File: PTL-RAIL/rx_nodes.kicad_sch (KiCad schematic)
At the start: 0 parts

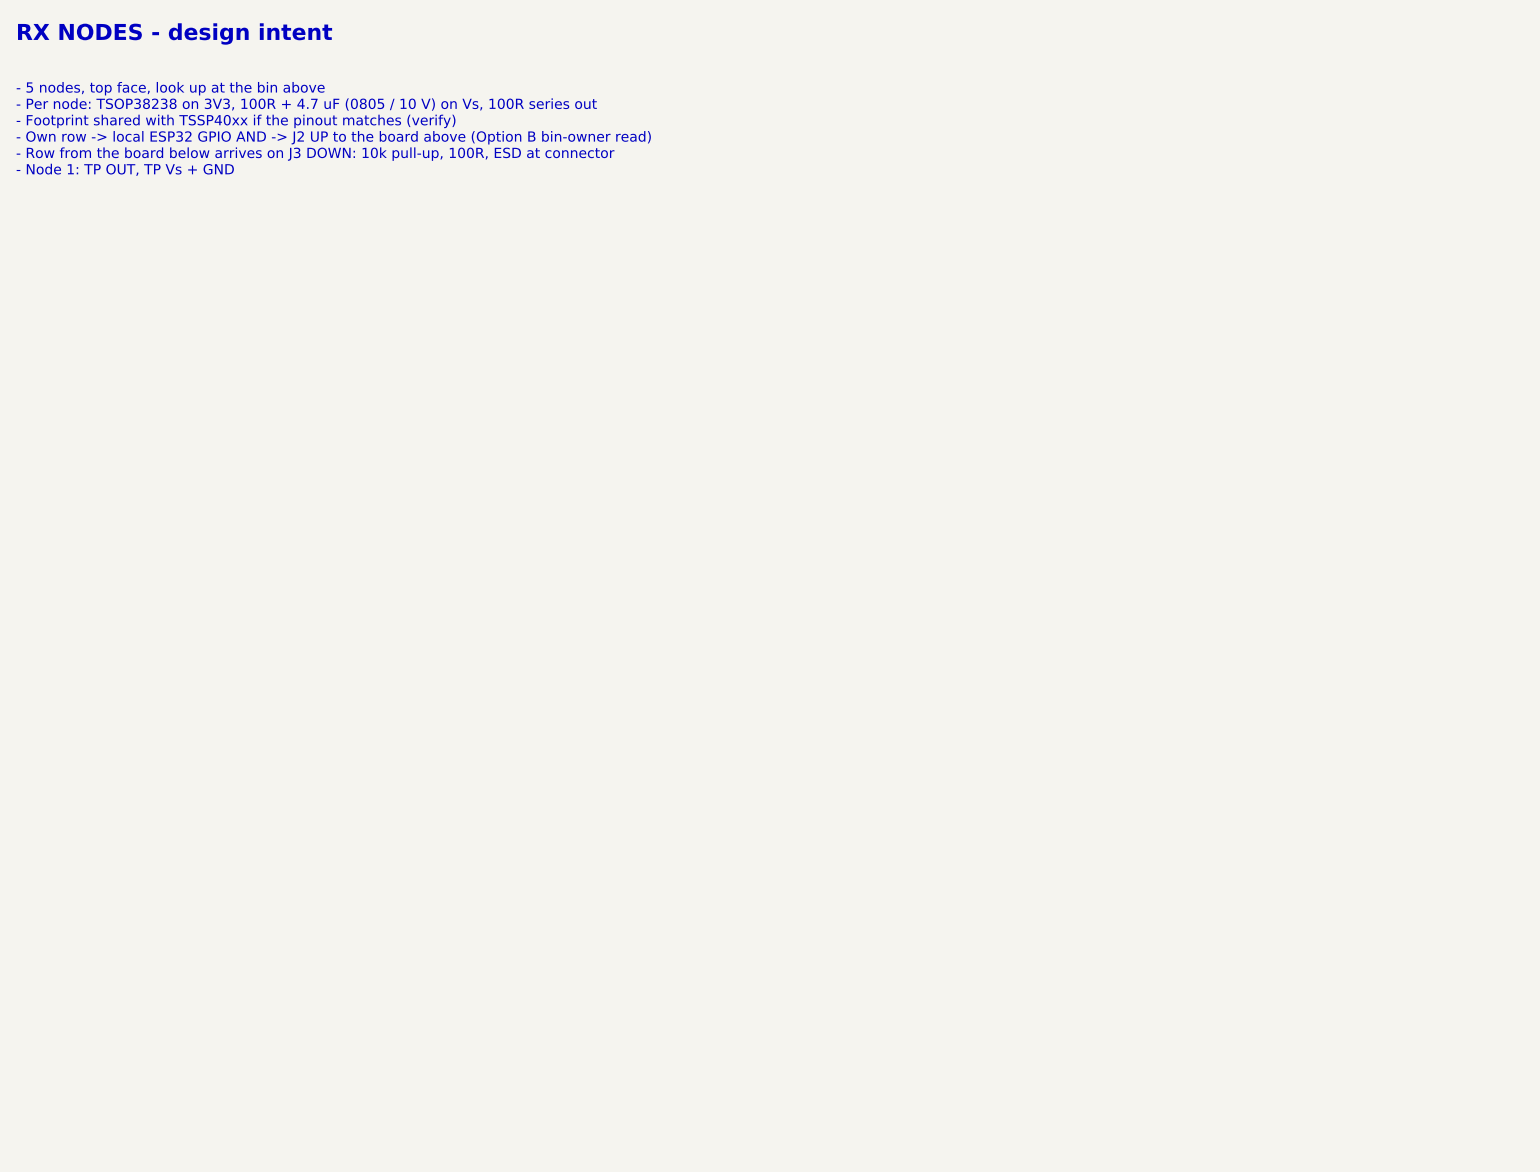
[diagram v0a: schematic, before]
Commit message: PTL-RAIL: LED row on top edge, TSOP row on bottom edge, node parts aligned at 84 mm pitch; J3/J4 10-way and J5/J6 4-way screw terminals
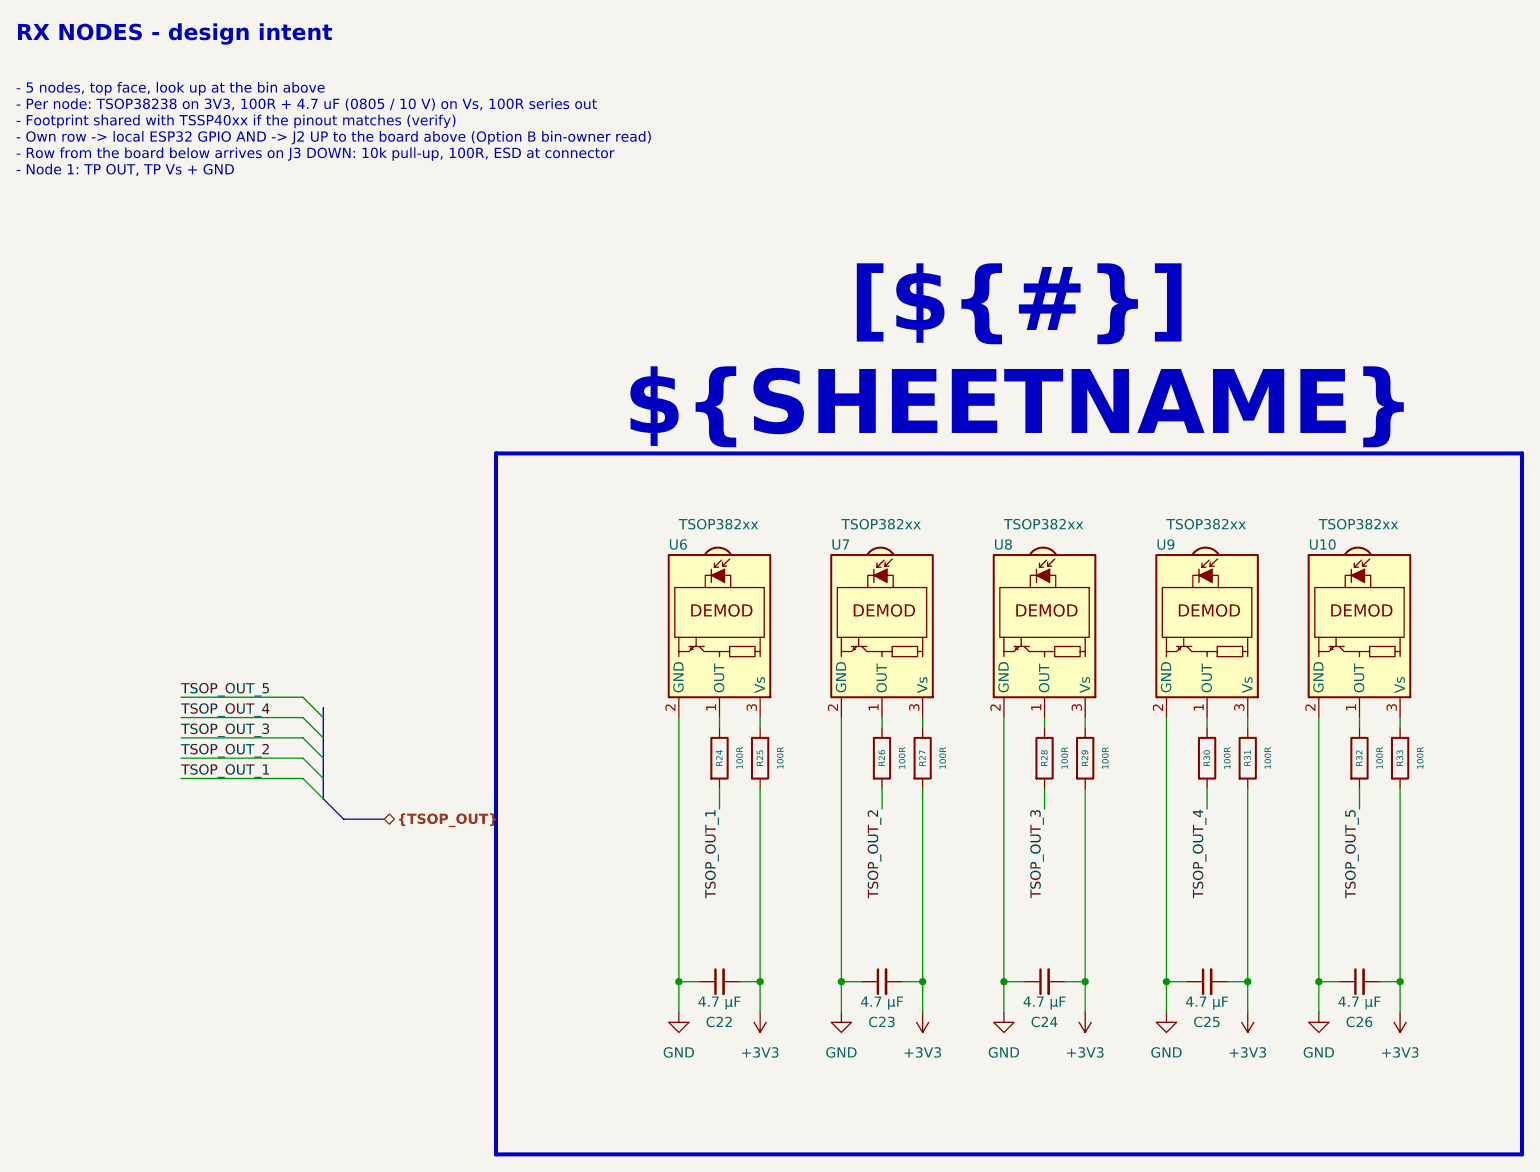
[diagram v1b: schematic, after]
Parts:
- added C22, C23, C24, C25, C26: 4.7 µF, Capacitor_SMD:C_0805_2012Metric, symbol Device:C_Small
- added R24, R25, R26, R27, R28, R29, R30, R31, R32, R33: 100R, Resistor_SMD:R_0805_2012Metric, symbol Device:R
- added U10, U6, U7, U8, U9: TSOP382xx, OptoDevice:Vishay_MINICAST-3Pin, symbol Interface_Optical:TSOP382xx
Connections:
- new net: R26.1, U7.1 (OUT)
- new net: R27.1, U7.3 (Vs)
- new net: R28.1, U8.1 (OUT)
- new net: R29.1, U8.3 (Vs)
- new net: R32.1, U10.1 (OUT)
- new net: R31.1, U9.3 (Vs)
- new net: R33.1, U10.3 (Vs)
- new net: R30.1, U9.1 (OUT)
- new net: R24.1, U6.1 (OUT)
- new net: R25.1, U6.3 (Vs)
- new net +3V3: C22.2, C23.2, C24.2, C25.2, C26.2, R25.2, R27.2, R29.2, R31.2, R33.2
- new net GND: C22.1, C23.1, C24.1, C25.1, C26.1, U10.2 (GND), U6.2 (GND), U7.2 (GND), U8.2 (GND), U9.2 (GND)
- new net TSOP_OUT_1: R24.2
- new net TSOP_OUT_2: R26.2
- new net TSOP_OUT_3: R28.2
- new net TSOP_OUT_4: R30.2
- new net TSOP_OUT_5: R32.2

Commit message: PTL-RAIL: TSOP Vs decoupling caps on the Vs node; place CAN, buttons, status LED and mounting holes
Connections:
- net +3V3: no longer C22.2, C23.2, C24.2, C25.2, C26.2
- net at R27.1, U7.3 (Vs): now also C23.2
- net at R29.1, U8.3 (Vs): now also C24.2
- net at R31.1, U9.3 (Vs): now also C25.2
- net at R33.1, U10.3 (Vs): now also C26.2
- net at R25.1, U6.3 (Vs): now also C22.2
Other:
- moved on the sheet: R25, R27, R29, R31, R33

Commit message: PTL-RAIL rev A: normalize cap values, IO45 no-connect, README and docs
- Capacitor values unified: 0.1uF -> 100nF (C10, C16-C21, C27; now one
  BOM line with C5), '4.7 µF' -> 4.7uF (C22-C26)
- No-connect flag on U3 IO45 (ERC clean apart from 2 CAN label warnings)
- Zones refilled
- PTL-RAIL/README.md: board summary, pinouts, ESP32 pin map, test points,
  mounting, fab/assembly notes, production file list, rev A open issues
- Root README points to PTL-RAIL and the release assets
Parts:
- C22, C23, C24, C25, C26: value 4.7 µF -> 4.7uF
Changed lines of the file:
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@@
 			)
 		)
-		(property "Value" "4.7 µF"
+		(property "Value" "4.7uF"
 			(at 148.59 144.78 90)
 			(show_name no)
@@
 			)
 		)
-		(property "Value" "4.7 µF"
+		(property "Value" "4.7uF"
 			(at 128.27 144.78 90)
 			(show_name no)
@@
 			)
 		)
-		(property "Value" "4.7 µF"
+		(property "Value" "4.7uF"
 			(at 107.95 144.78 90)
 			(show_name no)
@@
 			)
 		)
-		(property "Value" "4.7 µF"
+		(property "Value" "4.7uF"
 			(at 168.91 144.78 90)
 			(show_name no)
@@
 			)
 		)
-		(property "Value" "4.7 µF"
+		(property "Value" "4.7uF"
 			(at 187.96 144.78 90)
 			(show_name no)
